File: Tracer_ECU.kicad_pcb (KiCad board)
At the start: 4 copper layers, 82 x 60 mm, 165 parts, among them IC1 R5F572TFADFP#30, IC2 MPU-6500, IC3 DRV8320HRTVR, IC4 DRV8320HRTVR, IC5 DRV8320HRTVR, J1 BAT, J10 ENC2, J11 SENS2, J13 SDC, J14 ENC3, J2 DBG, J3 SENS1, J4 MOT3, J5 MOT1, J6 LIGHIT, J8 MOT2, J9 ENC1, Q1 TJ60S04M3L, Q10 FDS6898A, Q11 FDS6898A, Q12 FDS6898A, Q2 FDS6898A, Q3 FDS6898A, Q4 FDS6898A, Q6 IRLML6344TRPBF, Q7 FDS6898A, Q8 FDS6898A, Q9 FDS6898A, SW1 SW_SPDT, SW2 SW_Push, SW4 SW_Push, SW5 SW_Push, U1 NJM2732, U2 AZ1117-3.3, Y1 CSTNE20M

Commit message: PCBレイアウト修正
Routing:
- net Mot.1_SLA: vias 172 -> 173

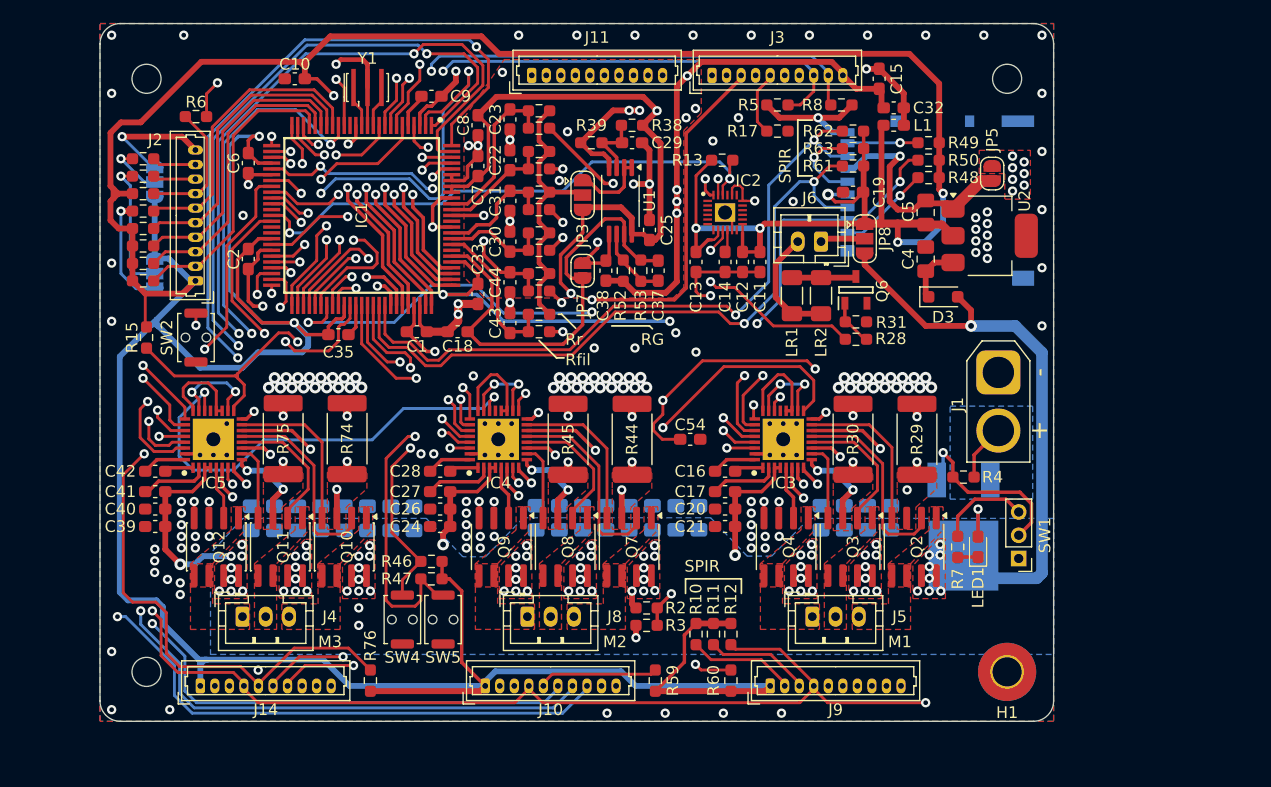
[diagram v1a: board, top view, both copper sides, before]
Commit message: 回路修正完了(2相/3相選択版) 小型化のため最小ビア径0.45mm/最小配線幅0.2mmへ変更 レイアウト修正8割方完了．一旦コミット
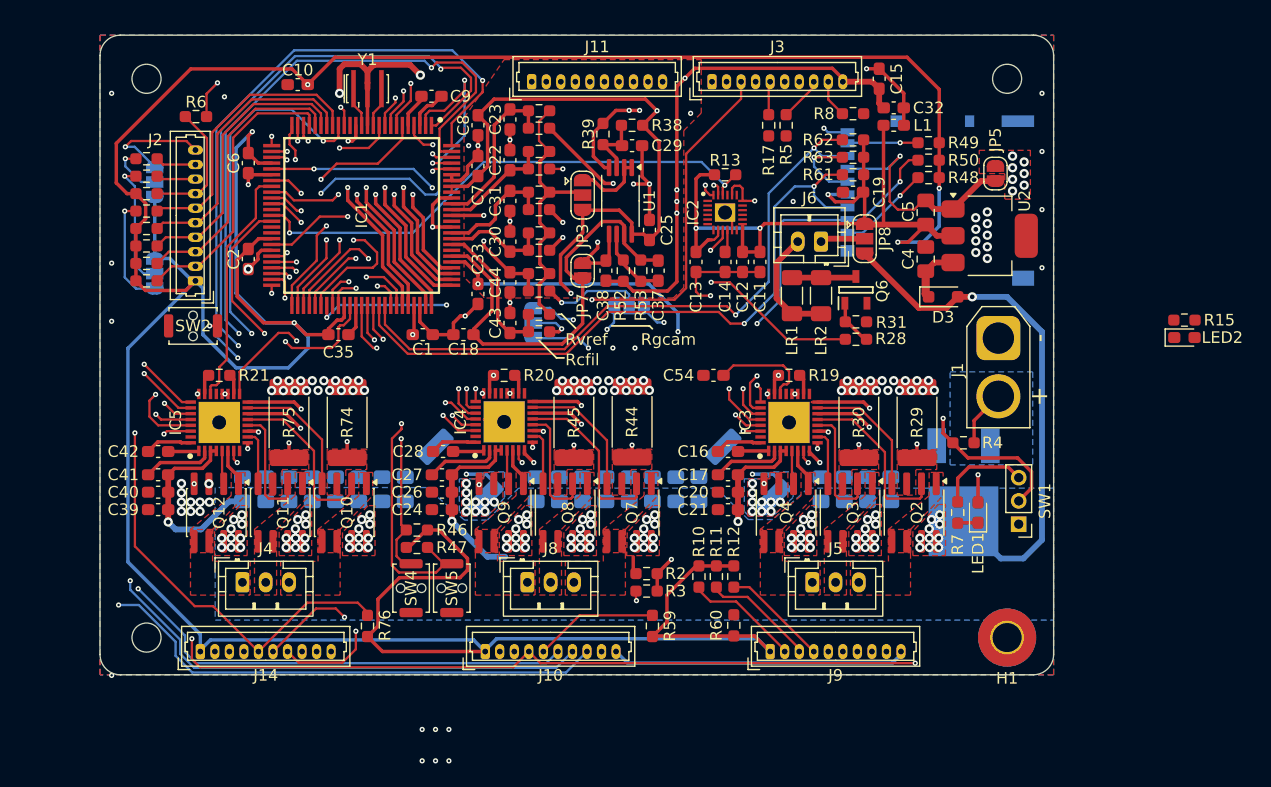
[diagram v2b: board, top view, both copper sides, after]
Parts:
- added JP2: Jumper, Jumper:SolderJumper-3_P1.3mm_Open_RoundedPad1.0x1.5mm, B.Cu at (134.0, 88.2)
- added JP4: Jumper, Jumper:SolderJumper-3_P1.3mm_Open_RoundedPad1.0x1.5mm, B.Cu at (125.8, 89.8)
- added LED2: LED, LED_SMD:LED_0603_1608Metric_Pad1.05x0.95mm_HandSolder, F.Cu at (181.8, 91.0)
- added R16: 0.05/1W, Resistor_SMD:R_2512_6332Metric_Pad1.40x3.35mm_HandSolder, B.Cu at (144.2, 102.5)
- added R18: 0.05/1W, Resistor_SMD:R_2512_6332Metric_Pad1.40x3.35mm_HandSolder, B.Cu at (119.5, 102.5)
- added R19: 47k, Resistor_SMD:R_0603_1608Metric_Pad0.98x0.95mm_HandSolder, F.Cu at (147.8, 94.2)
- added R20: 47k, Resistor_SMD:R_0603_1608Metric_Pad0.98x0.95mm_HandSolder, F.Cu at (123.2, 94.2)
- added R21: 47k, Resistor_SMD:R_0603_1608Metric_Pad0.98x0.95mm_HandSolder, F.Cu at (98.8, 94.2)
- R24, R25, R26, R27, R40, R41, R42, R43, R70, R71, R72, R73: value 470 -> 470F
- R38, R39: value 10k -> 10kF
- R52: value X1 -> XF
- R53: value X2 -> XF
- moved R15 89.3 mm to (181.8, 89.5), turned to 0 degrees
- moved C54 5.85 mm to (141.2, 94.2), turned to 0 degrees
- moved R10 4.96 mm to (140.0, 111.5)
- moved R11 4.96 mm to (141.5, 111.5)
- moved R12 4.96 mm to (143.0, 111.5)
- moved R60 4.76 mm to (143.0, 115.8)
- moved R59 4.71 mm to (136.0, 115.8)
- moved R76 4.71 mm to (111.5, 115.8)
- moved R46 2.98 mm to (115.8, 107.5)
- moved R47 2.98 mm to (115.8, 109.0), turned to 0 degrees
- moved J10 2.95 mm to (121.6, 118.0)
- moved J14 2.95 mm to (97.1, 118.0)
- moved J9 2.95 mm to (146.1, 118.0)
- moved H1 2.95 mm to (166.5, 116.8)
- moved J1 2.95 mm to (165.8, 91.0)
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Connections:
- C10 pad 2: Mot.1_SLA -> Mot.3_SLA
- C11 pad 2: Mot.1_SLA -> Mot.3_SLA
- C12 pad 2: Mot.1_SLA -> Mot.3_SLA
- C13 pad 2: Mot.1_SLA -> Mot.3_SLA
- C14 pad 2: Mot.1_SLA -> Mot.3_SLA
- C19 pad 2: Mot.1_SLA -> Mot.3_SLA
- C2 pad 2: Mot.1_SLA -> Mot.3_SLA
- C20 pad 1: Mot.1_SLA -> Mot.3_SLA
- C21 pad 1: Mot.1_SLA -> Mot.3_SLA
- C22 pad 2: Mot.1_SLA -> Mot.3_SLA
- C23 pad 2: Mot.1_SLA -> Mot.3_SLA
- C24 pad 1: Mot.1_SLA -> Mot.3_SLA
- C26 pad 1: Mot.1_SLA -> Mot.3_SLA
- C3 pad 2: Mot.1_SLA -> Mot.3_SLA
- C30 pad 2: Mot.1_SLA -> Mot.3_SLA
- C31 pad 2: Mot.1_SLA -> Mot.3_SLA
- C34 pad 2: Mot.1_SLA -> Mot.3_SLA
- C35 pad 2: Mot.1_SLA -> Mot.3_SLA
- C36 pad 2: Mot.1_SLA -> Mot.3_SLA
- C39 pad 1: Mot.1_SLA -> Mot.3_SLA
- C4 pad 2: Mot.1_SLA -> Mot.3_SLA
- C40 pad 1: Mot.1_SLA -> Mot.3_SLA
- C43 pad 2: Mot.1_SLA -> Mot.3_SLA
- C44 pad 2: Mot.1_SLA -> Mot.3_SLA
- C45 pad 2: Mot.1_SLA -> Mot.3_SLA
- C46 pad 2: Mot.1_SLA -> Mot.3_SLA
- C47 pad 2: Mot.1_SLA -> Mot.3_SLA
- C48 pad 2: Mot.1_SLA -> Mot.3_SLA
- C49 pad 2: Mot.1_SLA -> Mot.3_SLA
- C5 pad 2: Mot.1_SLA -> Mot.3_SLA
- C50 pad 2: Mot.1_SLA -> Mot.3_SLA
- C51 pad 2: Mot.1_SLA -> Mot.3_SLA
- C52 pad 2: Mot.1_SLA -> Mot.3_SLA
- C53 pad 2: Mot.1_SLA -> Mot.3_SLA
- C54 pad 1: Mot.1_SLA -> Mot.3_SLA
- C55 pad 2: Mot.1_SLA -> Mot.3_SLA
- C56 pad 2: Mot.1_SLA -> Mot.3_SLA
- C57 pad 2: Mot.1_SLA -> Mot.3_SLA
- C58 pad 2: Mot.1_SLA -> Mot.3_SLA
- C59 pad 2: Mot.1_SLA -> Mot.3_SLA
- C6 pad 2: Mot.1_SLA -> Mot.3_SLA
- C60 pad 2: Mot.1_SLA -> Mot.3_SLA
- C61 pad 2: Mot.1_SLA -> Mot.3_SLA
- C62 pad 2: Mot.1_SLA -> Mot.3_SLA
- C9 pad 2: Mot.1_SLA -> Mot.3_SLA
- H1 pad 1: Mot.1_SLA -> Mot.3_SLA
- IC1 pad 12: Mot.1_SLA -> Mot.3_SLA
- IC1 pad 3: Mot.1_SLA -> Mot.3_SLA
- IC1 pad 31: Mot.1_SLA -> Mot.3_SLA
- IC1 pad 44: Mot.1_SLA -> Mot.3_SLA
- IC1 pad 62: Mot.1_SLA -> Mot.3_SLA
- IC1 pad 86: Mot.1_SLA -> Mot.3_SLA
- IC1 pad 91: Mot.1_SLA -> Mot.3_SLA
- IC2 pad 11: Mot.1_SLA -> Mot.3_SLA
- IC2 pad 18: Mot.1_SLA -> Mot.3_SLA
- IC2 pad 20: Mot.1_SLA -> Mot.3_SLA
- IC2 pad 25: Mot.1_SLA -> Mot.3_SLA
- IC3 pad 18: GNDA -> Net-(IC3-MODE)
- IC3 pad 31: Mot.1_SLA -> Mot.3_SLA
- IC3 pad 33: Mot.1_SLA -> Mot.3_SLA
- IC3 pad 8: Mot.1_SLA -> M1_RU+
- IC4 pad 18: GNDA -> Net-(IC4-MODE)
- IC4 pad 31: Mot.1_SLA -> Mot.3_SLA
- IC4 pad 33: Mot.1_SLA -> Mot.3_SLA
- IC4 pad 8: Mot.1_SLA -> M2_RU+
- IC5 pad 18: GNDA -> Net-(IC5-MODE)
- IC5 pad 31: Mot.1_SLA -> Mot.3_SLA
- IC5 pad 33: Mot.1_SLA -> Mot.3_SLA
- IC5 pad 8: Mot.1_SLA -> Mot.3_SLA
- J1 pad 1: Mot.1_SLA -> Mot.3_SLA
- J10 pad 10: Mot.1_SLA -> Mot.3_SLA
- J13 pad 6: Mot.1_SLA -> Mot.3_SLA
- J13 pad 9: Mot.1_SLA -> Mot.3_SLA
- J14 pad 10: Mot.1_SLA -> Mot.3_SLA
- J2 pad 10: Mot.1_SLA -> Mot.3_SLA
- J9 pad 10: Mot.1_SLA -> Mot.3_SLA
- JP1 pad 1: Mot.1_SLA -> Mot.3_SLA
- JP5 pad 1: Mot.1_SLA -> Mot.3_SLA
- JP6 pad 1: Mot.1_SLA -> Mot.3_SLA
- Q12 pad 3: Mot.1_SLA -> Mot.3_SLA
- Q4 pad 3: Mot.1_SLA -> M1_RU+
- Q6 pad 2: Mot.1_SLA -> Mot.3_SLA
- Q9 pad 3: Mot.1_SLA -> M2_RU+
- R15 pad 2: IRQ15 -> Net-(LED2-A)
- R17 pad 2: Mot.1_SLA -> Mot.3_SLA
- R29 pad 2: Mot.1_SLA -> Mot.3_SLA
- R30 pad 2: Mot.1_SLA -> Mot.3_SLA
- R31 pad 1: Mot.1_SLA -> Mot.3_SLA
- R44 pad 2: Mot.1_SLA -> Mot.3_SLA
- R45 pad 2: Mot.1_SLA -> Mot.3_SLA
- R5 pad 2: Mot.1_SLA -> Mot.3_SLA
- R56 pad 2: Mot.1_SLA -> Mot.3_SLA
- R7 pad 2: Mot.1_SLA -> Mot.3_SLA
- R72 pad 1: Mot.3_SLC -> Net-(JP4-C)
- R73 pad 1: Mot.3_SLB -> Net-(JP2-C)
- R74 pad 2: Mot.1_SLA -> Mot.3_SLA
- R75 pad 2: Mot.1_SLA -> Mot.3_SLA
- R8 pad 2: Mot.1_SLA -> Mot.3_SLA
- SW1 pad 3: Mot.1_SLA -> Mot.3_SLA
- SW2 pad 1: Mot.1_SLA -> Mot.3_SLA
- SW4 pad 2: Mot.1_SLA -> Mot.3_SLA
- SW5 pad 2: Mot.1_SLA -> Mot.3_SLA
- U2 pad 1: Mot.1_SLA -> Mot.3_SLA
- Y1 pad 2: Mot.1_SLA -> Mot.3_SLA
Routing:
- net Mot.1_SLA: track 164.7 -> 0.00 mm, vias 173 -> 0
- net Mot.3_SLA: track 0.00 -> 160.6 mm, vias 0 -> 102
- net PB2(GD_EN): track 104.6 -> 29.5 mm, vias 6 -> 0
- net IRQ15: track 92.6 -> 18.4 mm, vias 4 -> 2
- net M1_RU+: track 0.00 -> 32.5 mm, vias 0 -> 12
- net M2_RU+: track 0.00 -> 21.1 mm, vias 0 -> 12
- net GNDA: track 181.0 -> 160.8 mm, vias 31 -> 22
- net Mot.3_SLB: track 42.2 -> 22.5 mm, vias 4 -> 3
- net Mot.3_SLC: track 40.6 -> 26.7 mm, vias 4 -> 3
- net Mot.3_SHA: track 14.6 -> 3.20 mm, vias 1 -> 0
- net Mot.1_SHA: track 14.6 -> 3.20 mm, vias 1 -> 0
- net Mot.2_SHA: track 14.6 -> 3.25 mm, vias 1 -> 0
- net AN201: track 57.8 -> 46.9 mm
- net Net-(JP2-C): track 0.00 -> 10.2 mm, vias 0 -> 1
- net RSPCKA: track 193.4 -> 183.5 mm
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- added copper zone on B.Cu, net M1_RU+
- added copper zone on F.Cu, net M1_RU+
- added copper zone on B.Cu, net M2_RU+
- added copper zone on F.Cu, net M2_RU+
- added copper zone on B.Cu, net Mot.3_SLA
- added copper zone on F.Cu, net Mot.3_SLA
- added copper zone on In1.Cu, net Mot.3_SLA
- removed copper zone on B.Cu, net Mot.1_SLA
- removed copper zone on F.Cu, net Mot.1_SLA
- removed copper zone on In1.Cu, net Mot.1_SLA
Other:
- board size 82 x 60 mm -> 82 x 55 mm
- board text added: "EMLE"
- board text added: "GND"
- board text added: "MD"
- board text added: "Rcfil"
- board text added: "Rgcam"
- board text added: "Rvref"
- board text added: "TCK"
- board text added: "TDI"
- board text added: "TDO"
- board text added: "TMS"
- board text added: "VCC"
- board text added: "nRES"
- board text added: "nTRES"
- board text removed: "M1"
- board text removed: "M2"
- board text removed: "M3"
- board text removed: "RG"
- board text removed: "Rfil"
- board text removed: "Rr"
- board text removed: "SPIR"

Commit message: アートワーク修正中． デバッグコネクタ周辺抵抗を1005M*4抵抗アレイに変更．
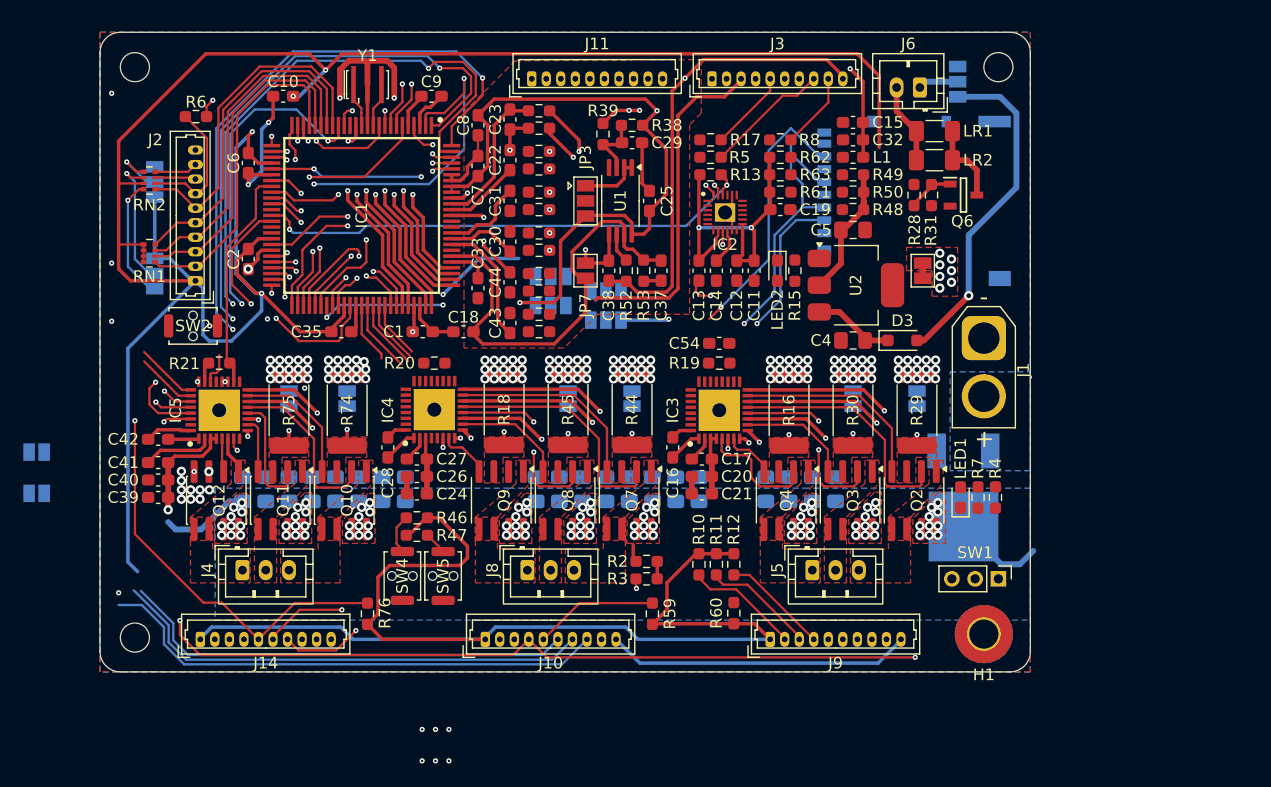
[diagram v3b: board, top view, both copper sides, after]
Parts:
- removed R1, R14, R54, R55, R56, R57, R58, R9: 4.7k, Resistor_SMD:R_0603_1608Metric_Pad0.98x0.95mm_HandSolder
- removed R40, R41, R42, R43, R70, R71, R72, R73: 470F, Resistor_SMD:R_0603_1608Metric_Pad0.98x0.95mm_HandSolder
- added JP10: Jumper, Jumper:SolderJumper-3_P1.3mm_Open_Pad1.0x1.5mm, B.Cu at (132.0, 87.0)
- added JP11: Jumper, Jumper:SolderJumper-2_P1.3mm_Open_Pad1.0x1.5mm, B.Cu at (83.0, 104.4)
- added JP12: Jumper, Jumper:SolderJumper-2_P1.3mm_Open_Pad1.0x1.5mm, B.Cu at (83.0, 100.8)
- added JP13: Jumper, Jumper:SolderJumper-2_P1.3mm_Open_Pad1.0x1.5mm, B.Cu at (128.8, 96.2)
- added JP14: Jumper, Jumper:SolderJumper-2_P1.3mm_Open_Pad1.0x1.5mm, B.Cu at (134.2, 96.2)
- added JP15: Jumper, Jumper:SolderJumper-2_P1.3mm_Open_Pad1.0x1.5mm, B.Cu at (153.2, 96.2)
- added JP16: Jumper, Jumper:SolderJumper-2_P1.3mm_Open_Pad1.0x1.5mm, B.Cu at (158.8, 96.2)
- added JP17: Jumper, Jumper:SolderJumper-2_P1.3mm_Open_Pad1.0x1.5mm, B.Cu at (104.8, 96.2)
- added JP18: Jumper, Jumper:SolderJumper-2_P1.3mm_Open_Pad1.0x1.5mm, B.Cu at (109.8, 96.2)
- added JP9: Jumper, Jumper:SolderJumper-3_P1.3mm_Open_Pad1.0x1.5mm, B.Cu at (127.2, 88.2)
- added R22: 1kF, Resistor_SMD:R_0603_1608Metric_Pad0.98x0.95mm_HandSolder, F.Cu at (126.2, 76.5)
- added R23: 1kF, Resistor_SMD:R_0603_1608Metric_Pad0.98x0.95mm_HandSolder, F.Cu at (126.2, 75.0)
- added R32: 1kF, Resistor_SMD:R_0603_1608Metric_Pad0.98x0.95mm_HandSolder, F.Cu at (126.2, 78.5)
- added R33: 1kF, Resistor_SMD:R_0603_1608Metric_Pad0.98x0.95mm_HandSolder, F.Cu at (126.2, 80.0)
- added R34: 1kF, Resistor_SMD:R_0603_1608Metric_Pad0.98x0.95mm_HandSolder, F.Cu at (126.2, 90.5)
- added R35: 1kF, Resistor_SMD:R_0603_1608Metric_Pad0.98x0.95mm_HandSolder, F.Cu at (126.2, 89.0)
- added R36: 1kF, Resistor_SMD:R_0603_1608Metric_Pad0.98x0.95mm_HandSolder, F.Cu at (126.2, 85.5)
- added R37: 1kF, Resistor_SMD:R_0603_1608Metric_Pad0.98x0.95mm_HandSolder, F.Cu at (126.2, 87.0)
- added RN1: 4.7k, My_Footprint_Lib:R_Array_Convex_4x0402, F.Cu at (92.8, 83.8)
- added RN2: 4.7k, My_Footprint_Lib:R_Array_Convex_4x0402, F.Cu at (92.8, 77.5)
- C22, C23, C30, C31, C43: value 1000p -> 0.1u
- JP1, JP2, JP3, JP4, JP6: footprint Jumper:SolderJumper-3_P1.3mm_Open_RoundedPad1.0x1.5mm -> Jumper:SolderJumper-3_P1.3mm_Open_Pad1.0x1.5mm
- JP5: footprint Jumper:SolderJumper-2_P1.3mm_Open_RoundedPad1.0x1.5mm -> Jumper:SolderJumper-2_P1.3mm_Bridged_Pad1.0x1.5mm
- JP7: footprint Jumper:SolderJumper-2_P1.3mm_Open_RoundedPad1.0x1.5mm -> Jumper:SolderJumper-2_P1.3mm_Open_Pad1.0x1.5mm
- JP8: footprint Jumper:SolderJumper-3_P1.3mm_Open_RoundedPad1.0x1.5mm -> Jumper:SolderJumper-3_P1.3mm_Open_Pad1.0x1.5mm; moved to B.Cu
- R16, R18: moved to F.Cu
- R24, R25, R26, R27: value 470F -> 1kF
- moved LED2 35.5 mm to (146.8, 85.2), turned to -90 degrees
- moved R15 33.8 mm to (148.2, 85.2), turned to -90 degrees
- moved LR1 18.7 mm to (160.2, 73.2), turned to 180 degrees
- moved J6 15.7 mm to (159.0, 69.5)
- moved JP8 15.7 mm to (162.2, 69.0)
- moved LR2 15.2 mm to (160.2, 75.8), turned to 180 degrees
- moved R28 13.4 mm to (158.5, 78.8), turned to 90 degrees
- moved R31 12.7 mm to (160.0, 78.8), turned to 90 degrees
- moved Q6 12.3 mm to (162.8, 78.8), turned to 0 degrees
- moved U2 12.3 mm to (153.5, 86.5)
- moved JP5 10.4 mm to (159.2, 85.2)
- moved C4 9.38 mm to (153.2, 91.2), turned to 180 degrees
- moved R27 9.00 mm to (126.2, 82.0), turned to 0 degrees
- moved JP2 7.20 mm to (127.2, 85.8)
- moved R48 7.06 mm to (153.2, 80.0)
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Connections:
- C22 pad 2: Mot.3_SLA -> PGAVSS0
- C23 pad 2: Mot.3_SLA -> PGAVSS0
- C30 pad 2: Mot.3_SLA -> PGAVSS1
- C31 pad 2: Mot.3_SLA -> PGAVSS1
- C43 pad 2: Mot.3_SLA -> PGAVSS1
- C44 pad 2: Mot.3_SLA -> PGAVSS0
- IC1 pad 86: Mot.3_SLA -> PGAVSS1
- IC1 pad 91: Mot.3_SLA -> PGAVSS0
- IC3 pad 8: M1_RU+ -> Mot.1_Ru+
- IC4 pad 8: M2_RU+ -> Mot.2_Ru+
- JP2 pad 3: M1_RU+ -> Mot.2_Ru+
- JP3 pad 2: Net-(JP3-C) -> unconnected-(JP3-C-Pad2)
- JP4 pad 3: M2_RU+ -> Mot.1_Ru+
- Q4 pad 3: M1_RU+ -> Mot.1_Ru+
- Q9 pad 3: M2_RU+ -> Mot.2_Ru+
- R16 pad 1: M1_RU+ -> Mot.1_Ru+
- R18 pad 1: M2_RU+ -> Mot.2_Ru+
- R24 pad 1: Net-(JP3-C) -> AN000
- R24 pad 2: AN001 -> Mot.1_SLB
- R25 pad 1: Net-(JP3-C) -> PGAVSS0
- R25 pad 2: AN000 -> Net-(JP15-A)
- R26 pad 1: Mot.1_SLC -> AN101
- R26 pad 2: AN001 -> Mot.2_SLC
- R27 pad 1: Mot.1_SLB -> PGAVSS1
- R27 pad 2: AN000 -> Net-(JP14-A)
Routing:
- net GNDA: track 160.8 -> 85.9 mm, vias 22 -> 11
- net Mot.3_SLA: track 160.6 -> 88.5 mm, vias 102 -> 127
- net VCC: track 398.6 -> 346.1 mm, vias 9 -> 7
- net Net-(JP16-A): track 0.00 -> 46.9 mm, vias 0 -> 1
- net AN201: track 46.9 -> 4.86 mm, vias 3 -> 0
- net SMOSI12: track 58.2 -> 23.6 mm, vias 2 -> 1
- net M1_RU+: track 32.5 -> 0.00 mm, vias 12 -> 0
- net SMISO12: track 57.6 -> 28.1 mm, vias 2 -> 1
- net +12V: track 96.0 -> 68.4 mm, vias 96 -> 93
- net P30: track 32.7 -> 7.22 mm, vias 2 -> 0
- net Mot.1_SLB: track 64.2 -> 38.8 mm
- net Net-(JP15-A): track 0.00 -> 25.4 mm, vias 0 -> 1
- net Mot.1_Ru+: track 0.00 -> 24.2 mm, vias 0 -> 3
- net Net-(JP3-C): track 24.0 -> 0.00 mm
- net AN216/IRQ7: track 56.7 -> 33.7 mm, vias 2 -> 1
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- added copper zone on F.Cu, net Mot.1_Ru+
- added copper zone on F.Cu, net Mot.2_Ru+
- removed copper zone on B.Cu, net M1_RU+
- removed copper zone on F.Cu, net M1_RU+
- removed copper zone on B.Cu, net M2_RU+
- removed copper zone on F.Cu, net M2_RU+
- removed copper zone on F.Cu, net Mot.1_SLB
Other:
- board size 82 x 55 mm -> 80 x 55 mm
- board text removed: "Rcfil"
- board text removed: "Rgcam"
- board text removed: "Rvref"

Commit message: DCバイアスを考慮しパワーＣサイズを変更． アートワーク修正中．
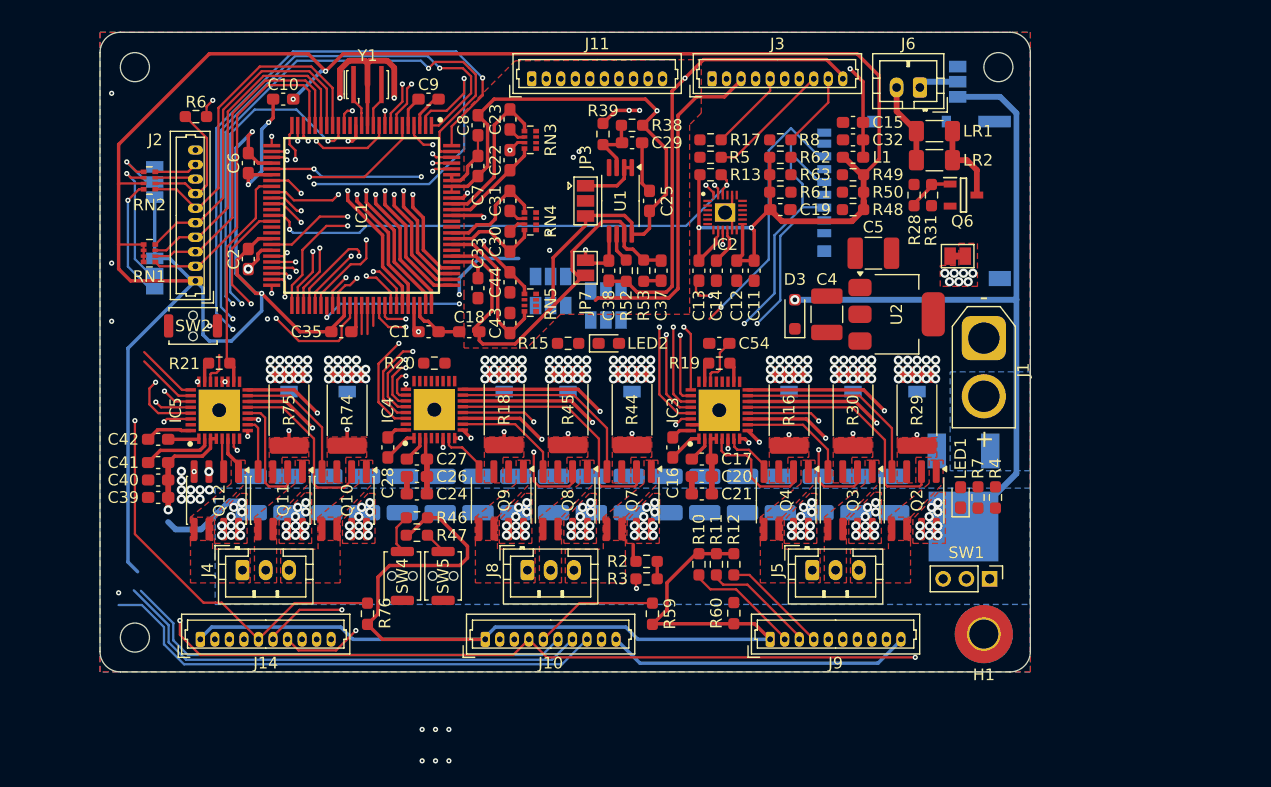
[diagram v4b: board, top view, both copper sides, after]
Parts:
- removed C61, C62: 22u, Capacitor_SMD:C_0805_2012Metric_Pad1.18x1.45mm_HandSolder
- removed R22, R23, R24, R25, R26, R27, R32, R33, R34, R35, R36, R37: 1kF, Resistor_SMD:R_0603_1608Metric_Pad0.98x0.95mm_HandSolder
- added RN3: 4.7k, My_Footprint_Lib:R_Array_Convex_4x0402, F.Cu at (125.5, 74.0)
- added RN4: 4.7k, My_Footprint_Lib:R_Array_Convex_4x0402, F.Cu at (125.5, 81.0)
- added RN5: 4.7k, My_Footprint_Lib:R_Array_Convex_4x0402, F.Cu at (125.5, 88.0)
- C22, C23, C30, C31, C43: value 0.1u -> 0.01u
- C3, C34, C36, C4, C45, C46, C47, C48, C49, C5, C50, C51, C52, C53, C55, C56, C57, C58, C59, C60: footprint Capacitor_SMD:C_0805_2012Metric_Pad1.18x1.45mm_HandSolder -> Capacitor_SMD:C_1210_3225Metric_Pad1.33x2.70mm_HandSolder
- C44: value 1000p -> 0.01
- moved JP11 65.4 mm to (147.8, 95.0), turned to 90 degrees
- moved JP12 40.6 mm to (123.2, 95.0), turned to 90 degrees
- moved R15 20.5 mm to (128.8, 91.5), turned to 0 degrees
- moved LED2 15.8 mm to (132.2, 91.5), turned to 0 degrees
- moved D3 9.52 mm to (148.2, 89.0), turned to 90 degrees
- moved C3 5.02 mm to (156.8, 104.5)
- moved C53 5.02 mm to (121.0, 104.5)
- moved U2 4.30 mm to (157.0, 89.0)
- moved C34 3.78 mm to (153.5, 104.5)
- moved C46 3.78 mm to (143.8, 104.5)
- moved C52 3.78 mm to (124.2, 104.5)
- moved C60 3.28 mm to (101.5, 104.5)
- moved JP5 3.25 mm to (162.2, 84.0), turned to 0 degrees
- moved C4 3.18 mm to (151.0, 89.0), turned to 90 degrees
- moved C55 3.03 mm to (117.8, 104.5)
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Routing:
- net Net-(JP16-A): track 46.9 -> 19.1 mm, vias 1 -> 0
- net +12V: track 68.4 -> 93.6 mm
- net Mot.3_SLA: track 88.5 -> 110.4 mm, vias 127 -> 126
- net Mot.1_Ru+: track 24.2 -> 6.04 mm, vias 3 -> 2
- net Mot.1_SLC: track 63.2 -> 54.5 mm, vias 3 -> 2
- net Mot.3_SLC: track 39.9 -> 31.5 mm
- net Net-(D3-K): track 7.06 -> 0.00 mm
- net MTIOC7B: track 19.7 -> 26.7 mm, vias 1 -> 2
- net MTIOC4D: track 49.4 -> 55.8 mm, vias 1 -> 2
- net VCC: track 346.1 -> 352.1 mm
- net IRQ15: track 19.9 -> 14.0 mm
- net Mot.1_SLB: track 38.8 -> 34.2 mm
- net MTIOC7A: track 22.1 -> 26.6 mm, vias 1 -> 2
- net PB2(GD_EN): track 20.0 -> 24.2 mm
- net P24: track 9.69 -> 5.45 mm
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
